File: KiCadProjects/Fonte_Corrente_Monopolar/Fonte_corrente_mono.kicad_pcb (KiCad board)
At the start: 2 copper layers, 90 x 100 mm, 3 parts, among them J2 tensoes, J3 sinais analogicos, J4 comunicacao / sinais digitais

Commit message: alterações Fonte de corrente
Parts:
- added R1: 100k, Resistor_THT:R_Axial_DIN0207_L6.3mm_D2.5mm_P7.62mm_Horizontal, F.Cu at (144.8, 86.0)
- added R2: 100k, Resistor_THT:R_Axial_DIN0207_L6.3mm_D2.5mm_P7.62mm_Horizontal, F.Cu at (144.8, 90.0)
- added R3: 100k, Resistor_THT:R_Axial_DIN0207_L6.3mm_D2.5mm_P7.62mm_Horizontal, F.Cu at (144.8, 94.0)
- added R4: 1k, Resistor_THT:R_Axial_DIN0207_L6.3mm_D2.5mm_P7.62mm_Horizontal, F.Cu at (144.8, 98.1)
- added R5: 100k, Resistor_THT:R_Axial_DIN0207_L6.3mm_D2.5mm_P7.62mm_Horizontal, F.Cu at (144.8, 102.2)
- added R6: 1k, Resistor_THT:R_Axial_DIN0207_L6.3mm_D2.5mm_P7.62mm_Horizontal, F.Cu at (144.8, 106.2)
- added Rg1: 3,3k, Resistor_THT:R_Axial_DIN0207_L6.3mm_D2.5mm_P7.62mm_Horizontal, F.Cu at (144.8, 110.2)
- added Rs1: 10, Resistor_THT:R_Axial_DIN0207_L6.3mm_D2.5mm_P7.62mm_Horizontal, F.Cu at (144.8, 114.3)
- added U1: AD828AN, AD828:N_8_ADI, F.Cu at (155.6, 86.0)
- added U2: INA128, Package_DIP:DIP-8_W7.62mm, F.Cu at (165.1, 106.7)
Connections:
- net +12V renamed VCC
- net -12V renamed VEE

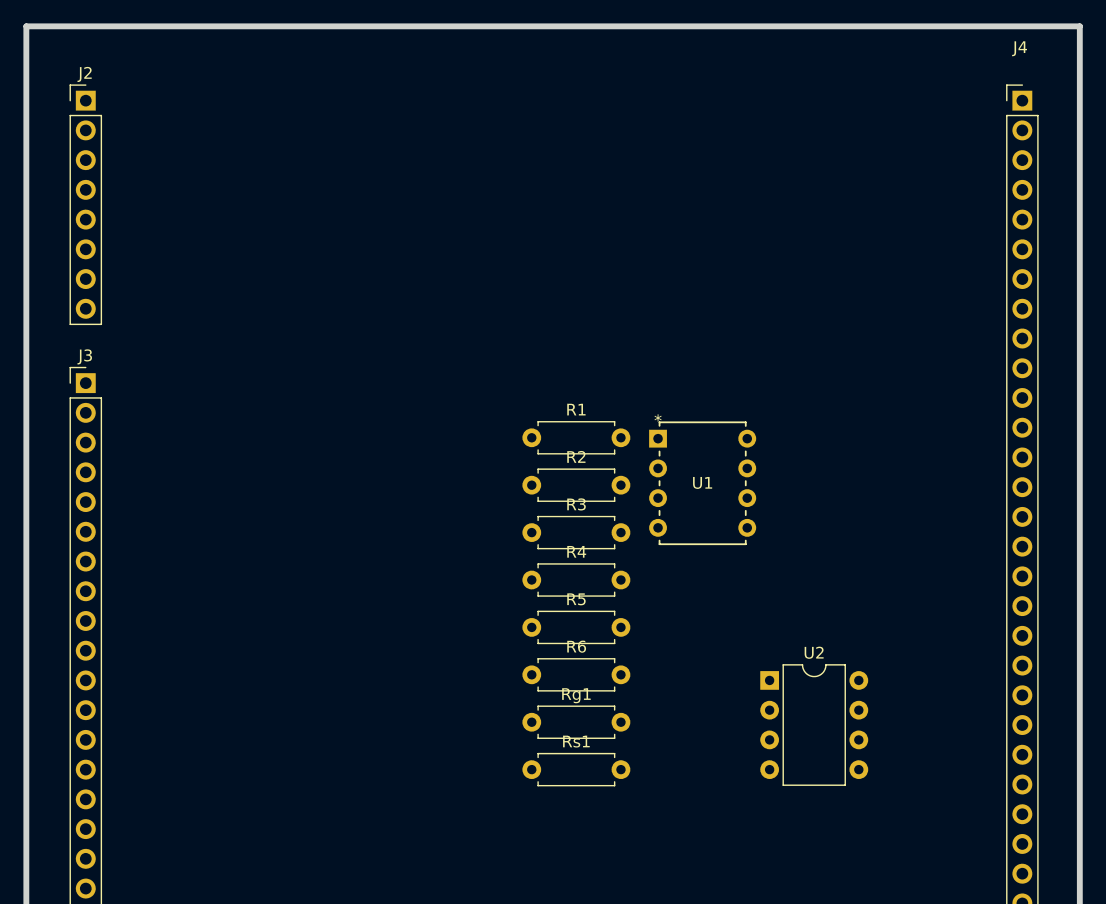
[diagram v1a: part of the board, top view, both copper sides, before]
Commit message: atribuição de footprint para todos os componentes da fonte de corrente monopolar
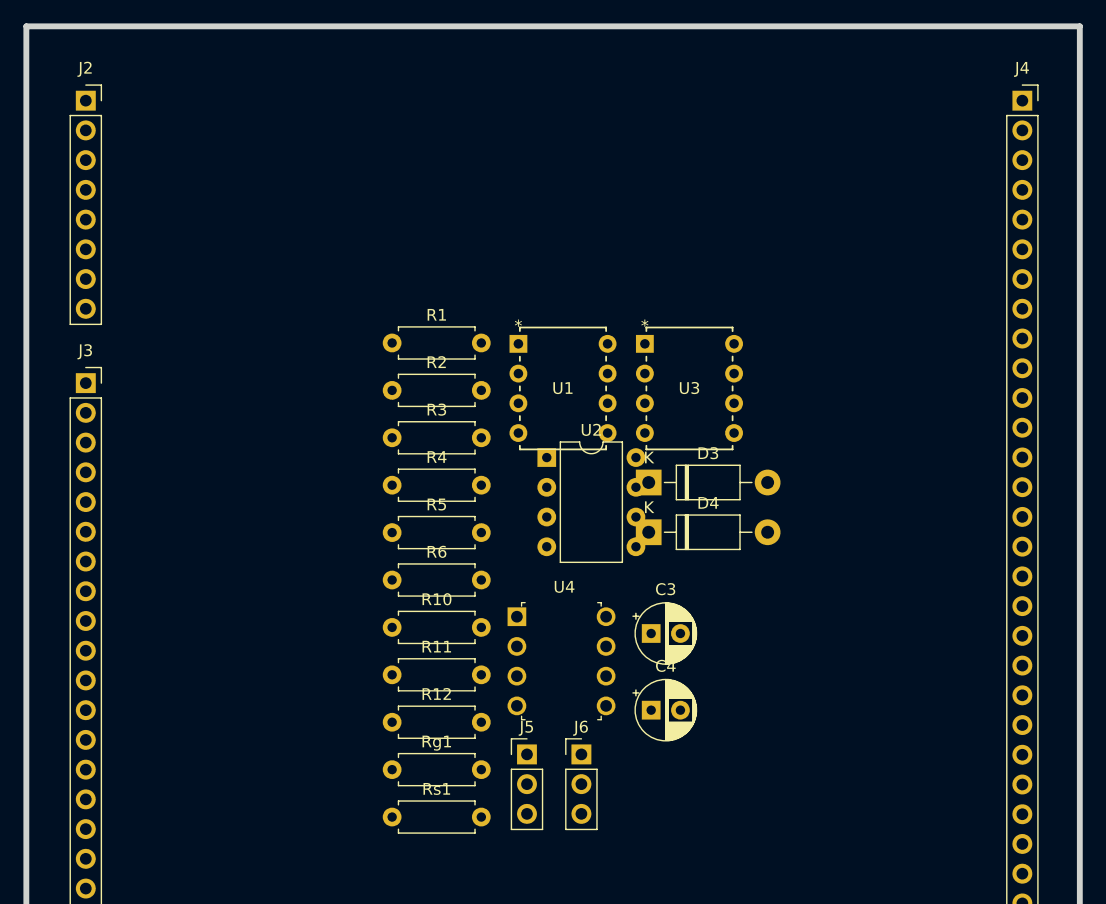
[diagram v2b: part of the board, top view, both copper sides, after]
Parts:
- added C3: 1 uF, Capacitor_THT:CP_Radial_D5.0mm_P2.50mm, F.Cu at (155.0, 102.7)
- added C4: 470 pF, Capacitor_THT:CP_Radial_D5.0mm_P2.50mm, F.Cu at (155.0, 109.2)
- added D3: 1N5819, Diode_THT:D_DO-41_SOD81_P10.16mm_Horizontal, F.Cu at (154.8, 89.8)
- added D4: 1N5819, Diode_THT:D_DO-41_SOD81_P10.16mm_Horizontal, F.Cu at (154.8, 94.0)
- added J5: Seleção circuito de condicionamento, Connector_PinHeader_2.54mm:PinHeader_1x03_P2.54mm_Vertical, F.Cu at (144.4, 113.0)
- added J6: Conn_01x03, Connector_PinHeader_2.54mm:PinHeader_1x03_P2.54mm_Vertical, F.Cu at (149.0, 113.0)
- added R10: 100k, Resistor_THT:R_Axial_DIN0207_L6.3mm_D2.5mm_P7.62mm_Horizontal, F.Cu at (132.9, 102.2)
- added R11: 100k, Resistor_THT:R_Axial_DIN0207_L6.3mm_D2.5mm_P7.62mm_Horizontal, F.Cu at (132.9, 106.2)
- added R12: 220, Resistor_THT:R_Axial_DIN0207_L6.3mm_D2.5mm_P7.62mm_Horizontal, F.Cu at (132.9, 110.2)
- added U3: AD828AN, AD828:N_8_ADI, F.Cu at (154.4, 77.9)
- added U4: TL071, digikey-footprints:DIP-8_W7.62mm, F.Cu at (143.5, 101.2)
- J2: footprint Connector_PinHeader_2.54mm:PinHeader_1x08_P2.54mm_Vertical -> Connector_PinSocket_2.54mm:PinSocket_1x08_P2.54mm_Vertical
- J3: footprint Connector_PinHeader_2.54mm:PinHeader_1x27_P2.54mm_Vertical -> Connector_PinSocket_2.54mm:PinSocket_1x27_P2.54mm_Vertical
- J4: footprint Connector_PinHeader_2.54mm:PinHeader_1x35_P2.54mm_Vertical -> Connector_PinSocket_2.54mm:PinSocket_1x35_P2.54mm_Vertical
- moved U2 26.9 mm to (146.1, 87.6)
- moved R1 14.4 mm to (132.9, 77.8)
- moved R5 14.4 mm to (132.9, 94.0)
- moved R6 14.4 mm to (132.9, 98.1)
- moved R2 14.4 mm to (132.9, 81.9)
- moved R3 14.4 mm to (132.9, 86.0)
- moved R4 14.4 mm to (132.9, 90.0)
- moved U1 14.4 mm to (143.6, 77.9)
- moved Rg1 12.6 mm to (132.9, 114.3)
- moved Rs1 12.6 mm to (132.9, 118.3)
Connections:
- U2 pad 6: Ampl1 -> V_INA

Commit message: autosave backup
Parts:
- removed U4: TL071, digikey-footprints:DIP-8_W7.62mm
- added J1: Vref, Connector_PinHeader_2.54mm:PinHeader_1x03_P2.54mm_Vertical, F.Cu at (131.6, 146.3)
- J5: value Seleção circuito de condicionamento -> Vref
- J6: value Conn_01x03 -> Pinos de verificação; footprint Connector_PinHeader_2.54mm:PinHeader_1x03_P2.54mm_Vertical -> Connector_PinHeader_2.54mm:PinHeader_1x14_P2.54mm_Horizontal
- U1, U3: footprint AD828:N_8_ADI -> AD828AN:N_8_ADI
- moved J6 61.3 mm to (130.3, 54.7), turned to 90 degrees
- moved Rg1 54.9 mm to (156.0, 64.5)
- moved U3 49.7 mm to (141.0, 125.7)
- moved Rs1 36.8 mm to (145.5, 83.8)
- moved J5 35.6 mm to (155.4, 146.8), turned to 90 degrees
- moved U1 28.7 mm to (120.7, 60.7)
- moved D3 27.4 mm to (143.8, 114.8)
- moved D4 27.4 mm to (143.8, 119.1)
- moved R11 27.0 mm to (125.2, 132.1)
- moved R10 27.0 mm to (125.2, 128.0)
- moved R12 27.0 mm to (125.2, 136.1)
- moved C3 25.5 mm to (160.8, 127.5)
- moved C4 25.5 mm to (160.8, 134.1)
- moved U2 20.6 mm to (156.0, 69.6)
- moved R1 7.89 mm to (134.4, 70.1)
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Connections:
- C3 pad 1: circuito_cond -> nó1
- C3 pad 2: Net-(C3-Pad2) -> nó2
- D3 pad 1: +5V -> Net-(D3-K)
- J4 pad 22: X9x10x_INC -> unconnected-(J4-Pin_22-Pad22)
- J4 pad 23: X9x10x_U/D -> unconnected-(J4-Pin_23-Pad23)
- J5 pad 1: Dual_AmpOp -> +3.3V
- J5 pad 2: V_INA -> Net-(D3-K)
- J5 pad 3: Single_AmpOp -> +5V
- J6 pad 1: out_dualAmpOp -> Ampl1
- J6 pad 2: circuito_cond -> nó2
- J6 pad 3: out_singleAmpOp -> nó1
- R10 pad 1: +5V -> Net-(J1-Pin_2)
- R10 pad 2: Net-(C3-Pad2) -> nó2
- R11 pad 1: Net-(C3-Pad2) -> nó2
- R12 pad 1: Net-(C3-Pad2) -> nó2
- U3 pad 5: Dual_AmpOp -> V_INA
- U3 pad 6: out_dualAmpOp -> nó1
- U3 pad 7: out_dualAmpOp -> nó1

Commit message: alterações PCB
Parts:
- moved J6 246.5 mm to (134.8, 301.1)
- moved U2 67.8 mm to (123.9, 129.4)
- moved RganhoINA1 67.1 mm to (123.9, 123.4)
- moved J1 66.3 mm to (173.8, 95.1)
- moved Rsentinela1 59.9 mm to (117.9, 137.0), turned to 90 degrees
- moved J5 47.8 mm to (173.8, 102.6)
- moved R11 45.8 mm to (171.0, 133.3), turned to -90 degrees
- moved R10 40.5 mm to (163.6, 115.0)
- moved R6 37.7 mm to (151.8, 70.1), turned to -90 degrees
- moved D3 33.5 mm to (176.4, 122.6), turned to 180 degrees
- moved R12 32.3 mm to (156.2, 127.1)
- moved D4 29.4 mm to (156.3, 145.6)
- moved R5 19.0 mm to (151.8, 91.0), turned to 90 degrees
- moved C3 14.3 mm to (156.3, 113.9), turned to -90 degrees
- moved U3 14.3 mm to (141.7, 111.4)
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- renumbered Rg1 to RganhoINA1, Rs1 to Rsentinela1
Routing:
- net SinA: track 0.00 -> 118.9 mm
- net out_corrente: track 0.00 -> 108.9 mm, vias 0 -> 2
- net Ampl1: track 0.00 -> 86.5 mm
- net Earth: track 0.00 -> 70.7 mm
- net Net-(U1-+IN2): track 0.00 -> 50.7 mm
- net nó2: track 0.00 -> 44.7 mm
- net Net-(J1-Pin_2): track 0.00 -> 40.4 mm
- net -9V: track 0.00 -> 34.3 mm
- net V_INA: track 0.00 -> 27.8 mm
- net Net-(U1--IN2): track 0.00 -> 24.1 mm
- net out_buffer: track 0.00 -> 23.5 mm
- net Net-(U1-OUT2): track 0.00 -> 22.5 mm
- net Net-(D3-K): track 0.00 -> 20.0 mm
- net I1: track 0.00 -> 18.3 mm
- net Net-(R3-Pad2): track 0.00 -> 7.52 mm
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
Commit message: autosave backup
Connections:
- net switch_out_1 renamed Net-(SW_kcd1-1)
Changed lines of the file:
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@@
   (net 77 "Net-(RganhoINA1-Pad1)")
   (net 78 "Net-(RganhoINA1-Pad2)")
-  (net 79 "switch_out_1")
+  (net 79 "Net-(SW_kcd1-1)")
   (net 80 "Net-(D3-K)")
   (net 81 "Net-(J1-Pin_2)")
@@
       (net 72 "out_buffer") (pinfunction "-IN1") (pintype "unspecified"))
     (pad "3" thru_hole circle (at 0 5.08) (size 1.524 1.524) (drill 0.8128) (layers "*.Cu" "*.Mask")
-      (net 79 "switch_out_1") (pinfunction "+IN1") (pintype "unspecified"))
+      (net 79 "Net-(SW_kcd1-1)") (pinfunction "+IN1") (pintype "unspecified"))
     (pad "4" thru_hole circle (at 0 7.62) (size 1.524 1.524) (drill 0.8128) (layers "*.Cu" "*.Mask")
       (net 4 "-9V") (pinfunction "V-") (pintype "power_in"))

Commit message: alterações PCB
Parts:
- removed J6: Pinos de verificação, Connector_PinHeader_2.54mm:PinHeader_1x14_P2.54mm_Horizontal
- added SW_kcd1: sw, Chave_Gangorra:chave gangorra 3 pinos, F.Cu at (122.0, 150.2)
- moved RganhoINA1 6.19 mm to (124.7, 117.3)
- moved U2 6.19 mm to (124.8, 123.2)
- moved Rsentinela1 6.19 mm to (118.8, 130.9)
- moved D4 5.91 mm to (155.9, 139.8)
- moved R11 3.87 mm to (169.8, 129.7)
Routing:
- net Earth: track 70.7 -> 242.9 mm
- net +3.3V: track 7.50 -> 175.3 mm, vias 0 -> 2
- net +9V: track 0.00 -> 152.0 mm, vias 0 -> 4
- net Net-(U1-+IN1): track 0.00 -> 136.8 mm
- net +5V: track 7.50 -> 131.2 mm
- net -9V: track 34.3 -> 126.9 mm, vias 0 -> 2
- net SinA: track 118.9 -> 31.8 mm, vias 0 -> 2
- net Ampl1: track 86.5 -> 74.5 mm
- net Sin1: track 0.00 -> 9.63 mm
- net Net-(U1-+IN2): track 50.7 -> 45.1 mm
- net Net-(J1-Pin_2): track 40.4 -> 35.5 mm
- net out_corrente: track 108.9 -> 104.7 mm
- net nó2: track 44.7 -> 40.9 mm
- net V_INA: track 27.8 -> 24.4 mm
- net (no net): vias 3 -> 0

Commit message: alterações PCB
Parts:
- renumbered U1 to U1-howland1, U3 to U3-cond1
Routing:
- net I1: track 18.3 -> 21.7 mm
- net nó1: track 7.16 -> 9.51 mm
- net +3.3V: track 175.3 -> 174.4 mm
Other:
- board text added: "+3.3V | +5.0V"
- board text added: "Fonte de corrente monopolar Howland aperfeiçoada v01 - 2023"

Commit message: alterações PCB: tamanho de pad
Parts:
- renumbered D3 to D1, D4 to D2
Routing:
- net Earth: track 242.6 -> 243.1 mm
